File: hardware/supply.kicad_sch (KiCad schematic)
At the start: 10 parts

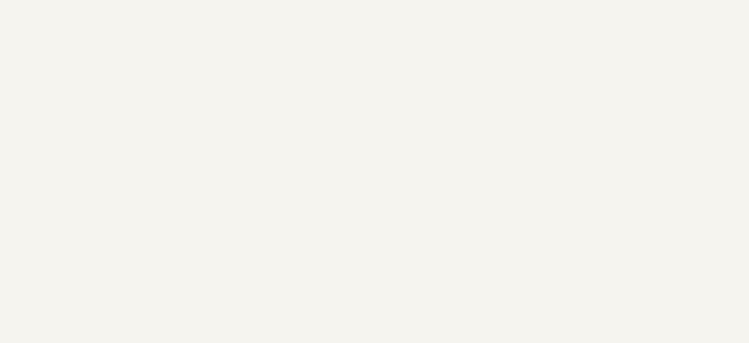
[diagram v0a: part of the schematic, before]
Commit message: hw: Add LDO regulator
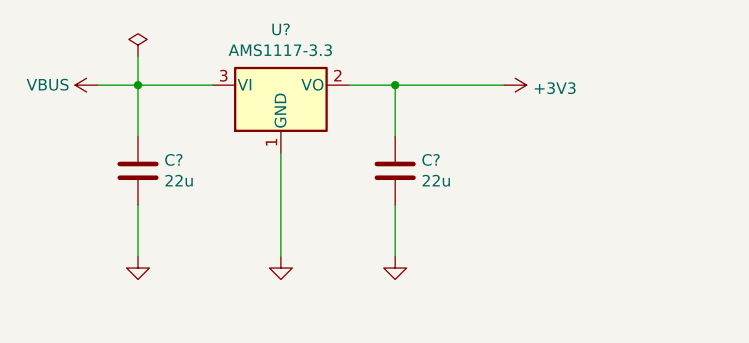
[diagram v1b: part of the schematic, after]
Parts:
- added C? (x2): 22u, Capacitor_SMD:C_1206_3216Metric_Pad1.33x1.80mm_HandSolder, symbol Device:C
- added U?: AMS1117-3.3, Package_TO_SOT_SMD:SOT-223-3_TabPin2, symbol Regulator_Linear:AMS1117-3.3
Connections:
- net +3V3: now also C?.1, U?.2 (VO)
- net GND: now also C?.2, C?.2, U?.1 (GND)
- new net VBUS: C?.1, U?.3 (VI)
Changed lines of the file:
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@@
   (junction (at 260.35 60.96) (diameter 0) (color 0 0 0 0)
   )
+  (junction (at 89.535 53.34) (diameter 0) (color 0 0 0 0)
+  )
+  (junction (at 118.11 53.34) (diameter 0) (color 0 0 0 0)
+  )
   (junction (at 237.49 60.96) (diameter 0) (color 0 0 0 0)
   )
@@
     (stroke (width 0) (type default) (color 0 0 0 0))
   )
+  (wire (pts (xy 118.11 66.675) (xy 118.11 72.39))
+    (stroke (width 0) (type default) (color 0 0 0 0))
+  )
+  (wire (pts (xy 85.09 53.34) (xy 89.535 53.34))
+    (stroke (width 0) (type default) (color 0 0 0 0))
+  )
   (wire (pts (xy 203.2 73.66) (xy 203.2 77.47))
     (stroke (width 0) (type default) (color 0 0 0 0))
@@
     (stroke (width 0) (type default) (color 0 0 0 0))
   )
+  (wire (pts (xy 118.11 53.34) (xy 118.11 59.055))
+    (stroke (width 0) (type default) (color 0 0 0 0))
+  )
   (wire (pts (xy 214.63 71.12) (xy 214.63 73.66))
     (stroke (width 0) (type default) (color 0 0 0 0))
@@
     (stroke (width 0) (type default) (color 0 0 0 0))
   )
+  (wire (pts (xy 89.535 53.34) (xy 97.79 53.34))
+    (stroke (width 0) (type default) (color 0 0 0 0))
+  )
   (wire (pts (xy 237.49 71.12) (xy 237.49 73.66))
     (stroke (width 0) (type default) (color 0 0 0 0))
@@
     (stroke (width 0) (type default) (color 0 0 0 0))
   )
+  (wire (pts (xy 89.535 59.055) (xy 89.535 53.34))
+    (stroke (width 0) (type default) (color 0 0 0 0))
+  )
+  (wire (pts (xy 105.41 60.96) (xy 105.41 72.39))
+    (stroke (width 0) (type default) (color 0 0 0 0))
+  )
   (wire (pts (xy 203.2 71.12) (xy 203.2 73.66))
     (stroke (width 0) (type default) (color 0 0 0 0))
@@
     (stroke (width 0) (type default) (color 0 0 0 0))
   )
+  (wire (pts (xy 118.11 53.34) (xy 130.175 53.34))
+    (stroke (width 0) (type default) (color 0 0 0 0))
+  )
   (wire (pts (xy 214.63 60.96) (xy 214.63 63.5))
     (stroke (width 0) (type default) (color 0 0 0 0))
@@
     (stroke (width 0) (type default) (color 0 0 0 0))
   )
+  (wire (pts (xy 89.535 66.675) (xy 89.535 72.39))
+    (stroke (width 0) (type default) (color 0 0 0 0))
+  )
   (wire (pts (xy 260.35 60.96) (xy 271.78 60.96))
     (stroke (width 0) (type default) (color 0 0 0 0))
@@
     (stroke (width 0) (type default) (color 0 0 0 0))
   )
+  (wire (pts (xy 113.03 53.34) (xy 118.11 53.34))
+    (stroke (width 0) (type default) (color 0 0 0 0))
+  )
   (wire (pts (xy 160.02 71.12) (xy 160.02 73.66))
+    (stroke (width 0) (type default) (color 0 0 0 0))
+  )
+  (wire (pts (xy 89.535 53.34) (xy 89.535 50.165))
     (stroke (width 0) (type default) (color 0 0 0 0))
   )
@@
     (effects (font (size 1.27 1.27)) (justify left bottom))
   )
+  (symbol (lib_id "Regulator_Linear:AMS1117-3.3") (at 105.41 53.34 0) (unit 1)
+    (in_bom yes) (on_board yes)
+    (property "Reference" "U?" (id 0) (at 105.41 47.1932 0))
+    (property "Value" "AMS1117-3.3" (id 1) (at 105.41 49.5046 0))
+    (property "Footprint" "Package_TO_SOT_SMD:SOT-223-3_TabPin2" (id 2) (at 105.41 48.26 0)
+      (effects (font (size 1.27 1.27)) hide)
+    )
+    (property "Datasheet" "http://www.advanced-monolithic.com/pdf/ds1117.pdf" (id 3) (at 107.95 59.69 0)
+      (effects (font (size 1.27 1.27)) hide)
+    )
+    (property "LCSC" "C6186" (id 4) (at 105.41 53.34 0)
+      (effects (font (size 1.27 1.27)) hide)
+    )
+    (pin "1")
+    (pin "2")
+    (pin "3")
+  )
   (symbol (lib_id "Device:C") (at 203.2 67.31 0) (unit 1)
     (in_bom yes) (on_board yes)
@@
     (pin "2")
   )
+  (symbol (lib_id "power:GND") (at 118.11 72.39 0) (unit 1)
+    (in_bom yes) (on_board yes)
+    (property "Reference" "#PWR?" (id 0) (at 118.11 78.74 0)
+      (effects (font (size 1.27 1.27)) hide)
+    )
+    (property "Value" "GND" (id 1) (at 118.237 76.7842 0)
+      (effects (font (size 1.27 1.27)) hide)
+    )
+    (property "Footprint" "" (id 2) (at 118.11 72.39 0)
+      (effects (font (size 1.27 1.27)) hide)
+    )
+    (property "Datasheet" "" (id 3) (at 118.11 72.39 0)
+      (effects (font (size 1.27 1.27)) hide)
+    )
+    (pin "1")
+  )
+  (symbol (lib_id "Device:C") (at 89.535 62.865 0) (unit 1)
+    (in_bom yes) (on_board yes)
+    (property "Reference" "C?" (id 0) (at 92.456 61.6966 0)
+      (effects (font (size 1.27 1.27)) (justify left))
+    )
+    (property "Value" "22u" (id 1) (at 92.456 64.008 0)
+      (effects (font (size 1.27 1.27)) (justify left))
+    )
+    (property "Footprint" "Capacitor_SMD:C_1206_3216Metric_Pad1.33x1.80mm_HandSolder" (id 2) (at 90.5002 66.675 0)
+      (effects (font (size 1.27 1.27)) hide)
+    )
+    (property "Datasheet" "~" (id 3) (at 89.535 62.865 0)
+      (effects (font (size 1.27 1.27)) hide)
+    )
+    (property "LCSC" "C12891" (id 4) (at 89.535 62.865 0)
+      (effects (font (size 1.27 1.27)) hide)
+    )
+    (pin "1")
+    (pin "2")
+  )
   (symbol (lib_id "Device:C") (at 160.02 67.31 0) (unit 1)
     (in_bom yes) (on_board yes)
@@
     (pin "2")
   )
+  (symbol (lib_id "power:VBUS") (at 85.09 53.34 90) (unit 1)
+    (in_bom yes) (on_board yes)
+    (property "Reference" "#PWR?" (id 0) (at 88.9 53.34 0)
+      (effects (font (size 1.27 1.27)) hide)
+    )
+    (property "Value" "VBUS" (id 1) (at 81.915 53.34 90)
+      (effects (font (size 1.27 1.27)) (justify left))
+    )
+    (property "Footprint" "" (id 2) (at 85.09 53.34 0)
+      (effects (font (size 1.27 1.27)) hide)
+    )
+    (property "Datasheet" "" (id 3) (at 85.09 53.34 0)
+      (effects (font (size 1.27 1.27)) hide)
+    )
+    (pin "1")
+  )
+  (symbol (lib_id "power:PWR_FLAG") (at 89.535 50.165 0) (unit 1)
+    (in_bom yes) (on_board yes)
+    (property "Reference" "#FLG?" (id 0) (at 89.535 48.26 0)
+      (effects (font (size 1.27 1.27)) hide)
+    )
+    (property "Value" "PWR_FLAG" (id 1) (at 89.535 45.7708 0)
+      (effects (font (size 1.27 1.27)) hide)
+    )
+    (property "Footprint" "" (id 2) (at 89.535 50.165 0)
+      (effects (font (size 1.27 1.27)) hide)
+    )
+    (property "Datasheet" "~" (id 3) (at 89.535 50.165 0)
+      (effects (font (size 1.27 1.27)) hide)
+    )
+    (pin "1")
+  )
   (symbol (lib_id "power:GND") (at 160.02 77.47 0) (unit 1)
     (in_bom yes) (on_board yes)
@@
       (effects (font (size 1.27 1.27)) hide)
     )
+    (pin "1")
+  )
+  (symbol (lib_id "Device:C") (at 118.11 62.865 0) (unit 1)
+    (in_bom yes) (on_board yes)
+    (property "Reference" "C?" (id 0) (at 121.031 61.6966 0)
+      (effects (font (size 1.27 1.27)) (justify left))
+    )
+    (property "Value" "22u" (id 1) (at 121.031 64.008 0)
+      (effects (font (size 1.27 1.27)) (justify left))
+    )
+    (property "Footprint" "Capacitor_SMD:C_1206_3216Metric_Pad1.33x1.80mm_HandSolder" (id 2) (at 119.0752 66.675 0)
+      (effects (font (size 1.27 1.27)) hide)
+    )
+    (property "Datasheet" "~" (id 3) (at 118.11 62.865 0)
+      (effects (font (size 1.27 1.27)) hide)
+    )
+    (property "LCSC" "C12891" (id 4) (at 118.11 62.865 0)
+      (effects (font (size 1.27 1.27)) hide)
+    )
+    (pin "1")
+    (pin "2")
+  )
+  (symbol (lib_id "power:GND") (at 89.535 72.39 0) (unit 1)
+    (in_bom yes) (on_board yes)
+    (property "Reference" "#PWR?" (id 0) (at 89.535 78.74 0)
+      (effects (font (size 1.27 1.27)) hide)
+    )
+    (property "Value" "GND" (id 1) (at 89.662 76.7842 0)
+      (effects (font (size 1.27 1.27)) hide)
+    )
+    (property "Footprint" "" (id 2) (at 89.535 72.39 0)
+      (effects (font (size 1.27 1.27)) hide)
+    )
+    (property "Datasheet" "" (id 3) (at 89.535 72.39 0)
+      (effects (font (size 1.27 1.27)) hide)
+    )
+    (pin "1")
+  )
+  (symbol (lib_id "power:+3V3") (at 130.175 53.34 270) (unit 1)
+    (in_bom yes) (on_board yes)
+    (property "Reference" "#PWR?" (id 0) (at 126.365 53.34 0)
+      (effects (font (size 1.27 1.27)) hide)
+    )
+    (property "Value" "+3V3" (id 1) (at 133.4262 53.721 90)
+      (effects (font (size 1.27 1.27)) (justify left))
+    )
+    (property "Footprint" "" (id 2) (at 130.175 53.34 0)
+      (effects (font (size 1.27 1.27)) hide)
+    )
+    (property "Datasheet" "" (id 3) (at 130.175 53.34 0)
+      (effects (font (size 1.27 1.27)) hide)
+    )
+    (pin "1")
+  )
+  (symbol (lib_id "power:GND") (at 105.41 72.39 0) (unit 1)
+    (in_bom yes) (on_board yes)
+    (property "Reference" "#PWR?" (id 0) (at 105.41 78.74 0)
+      (effects (font (size 1.27 1.27)) hide)
+    )
+    (property "Value" "GND" (id 1) (at 105.537 76.7842 0)
+      (effects (font (size 1.27 1.27)) hide)
+    )
+    (property "Footprint" "" (id 2) (at 105.41 72.39 0)
+      (effects (font (size 1.27 1.27)) hide)
+    )
+    (property "Datasheet" "" (id 3) (at 105.41 72.39 0)
+      (effects (font (size 1.27 1.27)) hide)
+    )
